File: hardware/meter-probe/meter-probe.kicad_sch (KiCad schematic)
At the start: 49 parts, among them J1 Cable, SW1 Sensor Button, U1 TSL2585, U2 USBLC6-2SC6, U3 MIC5365-1.8YC5, U4 FT260Q, U5 CAT24C08

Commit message: Change footprint of meter probe EEPROM
This change is for a smaller package, to better fit within enclosure
size constraints that limit height above the board on the front half.
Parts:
- U5: footprint Package_SO:SOIC-8_3.9x4.9mm_P1.27mm -> Package_SO:TSSOP-8_4.4x3mm_P0.65mm; Manufacturer PN CAT24C08WI-GT3 -> CAT24C08YI-GT3; Supplier PN CAT24C08WI-GT3CT-ND -> CAT24C08YI-GT3CT-ND
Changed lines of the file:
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@@
       (effects (font (size 1.27 1.27)) (justify left))
     )
-    (property "Footprint" "Package_SO:SOIC-8_3.9x4.9mm_P1.27mm" (at 149.86 129.54 0)
+    (property "Footprint" "Package_SO:TSSOP-8_4.4x3mm_P0.65mm" (at 149.86 129.54 0)
       (effects (font (size 1.27 1.27)) hide)
     )
@@
       (effects (font (size 1.27 1.27)) hide)
     )
-    (property "Description" "IC EEPROM 8KBIT I2C 400KHZ 8SOIC" (at 149.86 129.54 0)
+    (property "Description" "IC EEPROM 8KBIT I2C 8TSSOP" (at 149.86 129.54 0)
       (effects (font (size 1.27 1.27)) hide)
     )
@@
       (effects (font (size 1.27 1.27)) hide)
     )
-    (property "Manufacturer PN" "CAT24C08WI-GT3" (at 149.86 129.54 0)
+    (property "Manufacturer PN" "CAT24C08YI-GT3" (at 149.86 129.54 0)
       (effects (font (size 1.27 1.27)) hide)
     )
@@
       (effects (font (size 1.27 1.27)) hide)
     )
-    (property "Supplier PN" "CAT24C08WI-GT3CT-ND" (at 149.86 129.54 0)
+    (property "Supplier PN" "CAT24C08YI-GT3CT-ND" (at 149.86 129.54 0)
       (effects (font (size 1.27 1.27)) hide)
     )

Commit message: Move meter probe cable connector downward a bit
This required a fair amount of rerouting around the TVS components.
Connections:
- net at R12.1, SW1.2: now also D1.2 (K); no longer D1.1 (K)
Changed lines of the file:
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@@
   (junction (at 102.235 90.17) (diameter 0) (color 0 0 0 0)
   )
+  (junction (at 210.185 32.385) (diameter 0) (color 0 0 0 0)
+  )
   (junction (at 95.885 113.03) (diameter 0) (color 0 0 0 0)
   )
@@
   )
   (junction (at 162.56 61.595) (diameter 0) (color 0 0 0 0)
-  )
-  (junction (at 205.105 32.385) (diameter 0) (color 0 0 0 0)
   )
   (junction (at 134.62 27.305) (diameter 0) (color 0 0 0 0)
@@
   (no_connect (at 86.995 133.35))
   (no_connect (at 86.995 110.49))
-  (no_connect (at 210.185 35.56))
+  (no_connect (at 205.105 35.56))
   (no_connect (at 86.995 105.41))
   (no_connect (at 86.995 102.87))
@@
     (stroke (width 0) (type default))
   )
-  (wire (pts (xy 205.105 32.385) (xy 213.995 32.385))
+  (wire (pts (xy 199.39 32.385) (xy 210.185 32.385))
     (stroke (width 0) (type default))
   )
@@
     (stroke (width 0) (type default))
   )
-  (wire (pts (xy 199.39 32.385) (xy 205.105 32.385))
-    (stroke (width 0) (type default))
-  )
   (wire (pts (xy 62.865 158.115) (xy 73.025 158.115))
     (stroke (width 0) (type default))
@@
     (stroke (width 0) (type default))
   )
+  (wire (pts (xy 210.185 32.385) (xy 213.995 32.385))
+    (stroke (width 0) (type default))
+  )
   (wire (pts (xy 102.235 88.265) (xy 102.235 90.17))
     (stroke (width 0) (type default))
@@
   )
   (wire (pts (xy 44.45 29.845) (xy 25.4 29.845))
+    (stroke (width 0) (type default))
+  )
+  (wire (pts (xy 210.185 32.385) (xy 210.185 35.56))
     (stroke (width 0) (type default))
   )
@@
     (stroke (width 0) (type default))
   )
-  (wire (pts (xy 205.105 32.385) (xy 205.105 35.56))
-    (stroke (width 0) (type default))
-  )

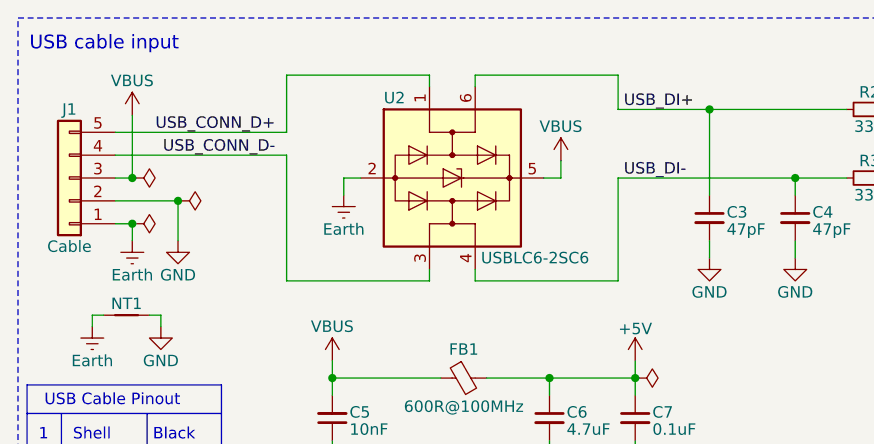
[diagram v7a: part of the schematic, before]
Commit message: Update meter probe board for library changes
Updated several custom footprints
Pulled in library changes for symbols and footprints
Fixed missing pull-up resistor on PCB layout
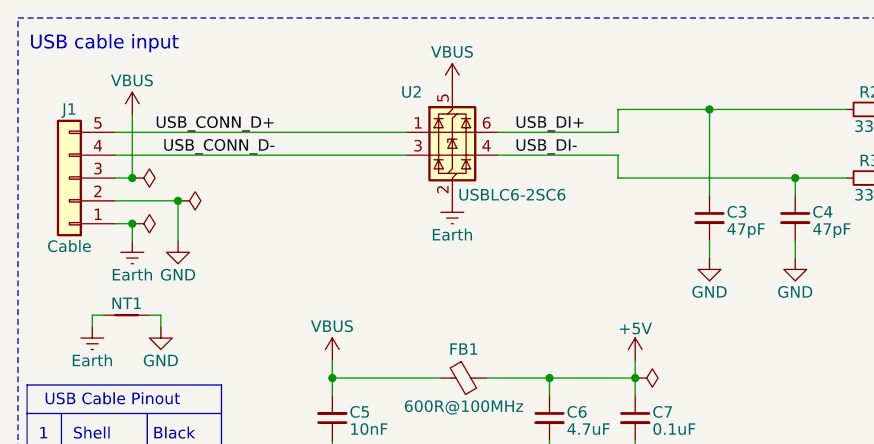
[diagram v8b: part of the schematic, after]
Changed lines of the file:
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@@
     (stroke (width 0) (type default))
   )
-  (wire (pts (xy 65.405 43.815) (xy 81.28 43.815))
-    (stroke (width 0) (type default))
-  )
   (wire (pts (xy 108.585 97.155) (xy 108.585 120.65))
     (stroke (width 0) (type default))
@@
     (stroke (width 0) (type default))
   )
-  (wire (pts (xy 52.705 32.385) (xy 50.8 32.385))
-    (stroke (width 0) (type default))
-  )
   (wire (pts (xy 186.69 32.385) (xy 186.69 34.925))
     (stroke (width 0) (type default))
@@
     (stroke (width 0) (type default))
   )
+  (wire (pts (xy 67.945 27.305) (xy 81.28 27.305))
+    (stroke (width 0) (type default))
+  )
   (wire (pts (xy 156.845 81.915) (xy 172.085 81.915))
     (stroke (width 0) (type default))
@@
     (stroke (width 0) (type default))
   )
-  (wire (pts (xy 65.405 20.955) (xy 81.28 20.955))
-    (stroke (width 0) (type default))
-  )
   (wire (pts (xy 62.865 158.115) (xy 62.865 159.385))
     (stroke (width 0) (type default))
   )
-  (wire (pts (xy 60.325 20.955) (xy 60.325 22.225))
-    (stroke (width 0) (type default))
-  )
   (wire (pts (xy 71.755 86.995) (xy 75.565 86.995))
     (stroke (width 0) (type default))
@@
     (stroke (width 0) (type default))
   )
-  (wire (pts (xy 163.83 27.305) (xy 161.925 27.305))
+  (wire (pts (xy 67.945 29.845) (xy 81.28 29.845))
     (stroke (width 0) (type default))
   )
-  (wire (pts (xy 44.45 20.955) (xy 60.325 20.955))
+  (wire (pts (xy 163.83 27.305) (xy 161.925 27.305))
     (stroke (width 0) (type default))
   )
@@
     (stroke (width 0) (type default))
   )
-  (wire (pts (xy 65.405 42.545) (xy 65.405 43.815))
-    (stroke (width 0) (type default))
-  )
   (wire (pts (xy 86.995 115.57) (xy 102.235 115.57))
     (stroke (width 0) (type default))
   )
-  (wire (pts (xy 44.45 27.305) (xy 25.4 27.305))
-    (stroke (width 0) (type default))
-  )
   (wire (pts (xy 30.48 47.625) (xy 30.48 48.895))
     (stroke (width 0) (type default))
@@
     (stroke (width 0) (type default))
   )
-  (wire (pts (xy 44.45 29.845) (xy 25.4 29.845))
+  (wire (pts (xy 25.4 29.845) (xy 57.785 29.845))
     (stroke (width 0) (type default))
   )
@@
     (stroke (width 0) (type default))
   )
+  (wire (pts (xy 81.28 29.845) (xy 81.28 32.385))
+    (stroke (width 0) (type default))
+  )
   (wire (pts (xy 145.415 61.595) (xy 145.415 71.755))
     (stroke (width 0) (type default))
@@
     (stroke (width 0) (type default))
   )
-  (wire (pts (xy 74.93 30.48) (xy 74.93 32.385))
-    (stroke (width 0) (type default))
-  )
   (wire (pts (xy 224.155 24.13) (xy 224.155 25.4))
     (stroke (width 0) (type default))
@@
     (stroke (width 0) (type default))
   )
-  (wire (pts (xy 60.325 43.815) (xy 60.325 42.545))
-    (stroke (width 0) (type default))
-  )
   (wire (pts (xy 234.315 160.655) (xy 236.22 160.655))
     (stroke (width 0) (type default))
@@
     (stroke (width 0) (type default))
   )
-  (wire (pts (xy 44.45 27.305) (xy 44.45 20.955))
-    (stroke (width 0) (type default))
-  )
   (wire (pts (xy 27.305 37.465) (xy 27.305 39.37))
     (stroke (width 0) (type default))
@@
     (stroke (width 0) (type default))
   )
+  (wire (pts (xy 25.4 27.305) (xy 57.785 27.305))
+    (stroke (width 0) (type default))
+  )
   (wire (pts (xy 95.885 90.17) (xy 102.235 90.17))
     (stroke (width 0) (type default))
@@
     (stroke (width 0) (type default))
   )
-  (wire (pts (xy 65.405 20.955) (xy 65.405 22.225))
-    (stroke (width 0) (type default))
-  )
   (wire (pts (xy 62.865 156.845) (xy 62.865 158.115))
     (stroke (width 0) (type default))
@@
     (stroke (width 0) (type default))
   )
-  (wire (pts (xy 44.45 43.815) (xy 60.325 43.815))
-    (stroke (width 0) (type default))
-  )
   (wire (pts (xy 156.845 120.015) (xy 160.02 120.015))
     (stroke (width 0) (type default))
@@
     (stroke (width 0) (type default))
   )
-  (wire (pts (xy 81.28 43.815) (xy 81.28 32.385))
+  (wire (pts (xy 81.28 27.305) (xy 81.28 24.765))
     (stroke (width 0) (type default))
   )
@@
     (stroke (width 0) (type default))
   )
-  (wire (pts (xy 50.8 32.385) (xy 50.8 34.29))
-    (stroke (width 0) (type default))
-  )
-  (wire (pts (xy 81.28 20.955) (xy 81.28 24.765))
-    (stroke (width 0) (type default))
-  )
   (wire (pts (xy 236.22 151.765) (xy 234.315 151.765))
     (stroke (width 0) (type default))
@@
     (stroke (width 0) (type default))
   )
-  (wire (pts (xy 74.93 32.385) (xy 73.025 32.385))
-    (stroke (width 0) (type default))
-  )
   (wire (pts (xy 151.765 37.465) (xy 151.765 38.1))
     (stroke (width 0) (type default))
@@
     (stroke (width 0) (type default))
   )
-  (wire (pts (xy 44.45 29.845) (xy 44.45 43.815))
-    (stroke (width 0) (type default))
-  )
   (wire (pts (xy 71.755 144.78) (xy 71.755 145.415))
     (stroke (width 0) (type default))
@@
     (effects (font (size 1.27 1.27)) (justify right bottom))
   )
-  (label "USB_DI+" (at 81.915 24.765 0) (fields_autoplaced)
+  (label "USB_DI+" (at 69.85 27.305 0) (fields_autoplaced)
     (effects (font (size 1.27 1.27)) (justify left bottom))
   )
-  (label "USB_DI-" (at 81.915 32.385 0) (fields_autoplaced)
+  (label "USB_DI-" (at 69.85 29.845 0) (fields_autoplaced)
     (effects (font (size 1.27 1.27)) (justify left bottom))
   )
@@
     )
   )
-  (symbol (lib_id "Power_Protection:USBLC6-2SC6") (at 62.865 32.385 270) (unit 1)
+  (symbol (lib_name "USBLC6-2SC6_1") (lib_id "Power_Protection:USBLC6-2SC6") (at 62.865 27.305 0) (unit 1)
     (in_bom yes) (on_board yes) (dnp no)
-    (property "Reference" "U2" (at 55.245 23.495 90)
+    (property "Reference" "U2" (at 57.15 22.86 0)
       (effects (font (size 1.27 1.27)) (justify left))
     )
-    (property "Value" "USBLC6-2SC6" (at 66.04 41.275 90)
+    (property "Value" "USBLC6-2SC6" (at 63.5 34.29 0)
       (effects (font (size 1.27 1.27)) (justify left))
     )
-    (property "Footprint" "Package_TO_SOT_SMD:SOT-23-6" (at 50.165 32.385 0)
+    (property "Footprint" "Package_TO_SOT_SMD:SOT-23-6" (at 62.865 40.005 0)
       (effects (font (size 1.27 1.27)) hide)
     )
-    (property "Datasheet" "https://www.st.com/resource/en/datasheet/usblc6-2.pdf" (at 71.755 37.465 0)
+    (property "Datasheet" "https://www.st.com/resource/en/datasheet/usblc6-2.pdf" (at 67.945 18.415 0)
       (effects (font (size 1.27 1.27)) hide)
     )
-    (property "Description" "TVS DIODE 5.25V 17V SOT23-6" (at 62.865 32.385 0)
+    (property "Description" "TVS DIODE 5.25V 17V SOT23-6" (at 62.865 27.305 0)
       (effects (font (size 1.27 1.27)) hide)
     )
-    (property "Manufacturer" "STMicroelectronics" (at 62.865 32.385 0)
+    (property "Manufacturer" "STMicroelectronics" (at 62.865 27.305 0)
       (effects (font (size 1.27 1.27)) hide)
     )
-    (property "Manufacturer PN" "USBLC6-2SC6" (at 62.865 32.385 0)
+    (property "Manufacturer PN" "USBLC6-2SC6" (at 62.865 27.305 0)
       (effects (font (size 1.27 1.27)) hide)
     )
-    (property "Supplier" "Digi-Key" (at 62.865 32.385 0)
+    (property "Supplier" "Digi-Key" (at 62.865 27.305 0)
       (effects (font (size 1.27 1.27)) hide)
     )
-    (property "Supplier PN" "497-5235-1-ND" (at 62.865 32.385 0)
+    (property "Supplier PN" "497-5235-1-ND" (at 62.865 27.305 0)
       (effects (font (size 1.27 1.27)) hide)
     )
@@
     )
   )
-  (symbol (lib_id "power:VBUS") (at 74.93 30.48 0) (mirror y) (unit 1)
+  (symbol (lib_id "power:VBUS") (at 62.865 22.225 0) (mirror y) (unit 1)
     (in_bom yes) (on_board yes) (dnp no)
-    (property "Reference" "#PWR020" (at 74.93 34.29 0)
+    (property "Reference" "#PWR020" (at 62.865 26.035 0)
       (effects (font (size 1.27 1.27)) hide)
     )
-    (property "Value" "VBUS" (at 74.93 26.67 0)
+    (property "Value" "VBUS" (at 62.865 18.415 0)
       (effects (font (size 1.27 1.27)))
     )
-    (property "Footprint" "" (at 74.93 30.48 0)
+    (property "Footprint" "" (at 62.865 22.225 0)
       (effects (font (size 1.27 1.27)) hide)
     )
-    (property "Datasheet" "" (at 74.93 30.48 0)
+    (property "Datasheet" "" (at 62.865 22.225 0)
       (effects (font (size 1.27 1.27)) hide)
     )
@@
     )
   )
-  (symbol (lib_id "power:Earth") (at 50.8 34.29 0) (mirror y) (unit 1)
+  (symbol (lib_id "power:Earth") (at 62.865 34.925 0) (mirror y) (unit 1)
     (in_bom yes) (on_board yes) (dnp no) (fields_autoplaced)
-    (property "Reference" "#PWR012" (at 50.8 40.64 0)
+    (property "Reference" "#PWR012" (at 62.865 41.275 0)
       (effects (font (size 1.27 1.27)) hide)
     )
-    (property "Value" "Earth" (at 50.8 38.1 0)
+    (property "Value" "Earth" (at 62.865 38.735 0)
       (effects (font (size 1.27 1.27)))
     )
-    (property "Footprint" "" (at 50.8 34.29 0)
+    (property "Footprint" "" (at 62.865 34.925 0)
       (effects (font (size 1.27 1.27)) hide)
     )
-    (property "Datasheet" "~" (at 50.8 34.29 0)
+    (property "Datasheet" "~" (at 62.865 34.925 0)
       (effects (font (size 1.27 1.27)) hide)
     )
-    (property "Description" "" (at 50.8 34.29 0)
+    (property "Description" "" (at 62.865 34.925 0)
       (effects (font (size 1.27 1.27)) hide)
     )
-    (property "Manufacturer" "" (at 50.8 34.29 0)
+    (property "Manufacturer" "" (at 62.865 34.925 0)
       (effects (font (size 1.27 1.27)) hide)
     )
-    (property "Manufacturer PN" "" (at 50.8 34.29 0)
+    (property "Manufacturer PN" "" (at 62.865 34.925 0)
       (effects (font (size 1.27 1.27)) hide)
     )
-    (property "Supplier" "" (at 50.8 34.29 0)
+    (property "Supplier" "" (at 62.865 34.925 0)
       (effects (font (size 1.27 1.27)) hide)
     )
-    (property "Supplier PN" "" (at 50.8 34.29 0)
+    (property "Supplier PN" "" (at 62.865 34.925 0)
       (effects (font (size 1.27 1.27)) hide)
     )
